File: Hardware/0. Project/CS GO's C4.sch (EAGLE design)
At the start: 47 parts, among them CN1 CELL--PHMC4-02, CN2 ICSP, CN4 TERMINAL-BLOCK-2P-5MM, CN5 TERMINAL-BLOCK-2P-5MM, Q1 NPN-BC817, Q3 N-FET-ENHANCEMENT-SQ2310, SW1 SPST-LATCH-PHMC4-02, U1 1117-3.3V, U4 PCF8574DW, U6 ATMEGA328P-PU, Y1 16 MHz

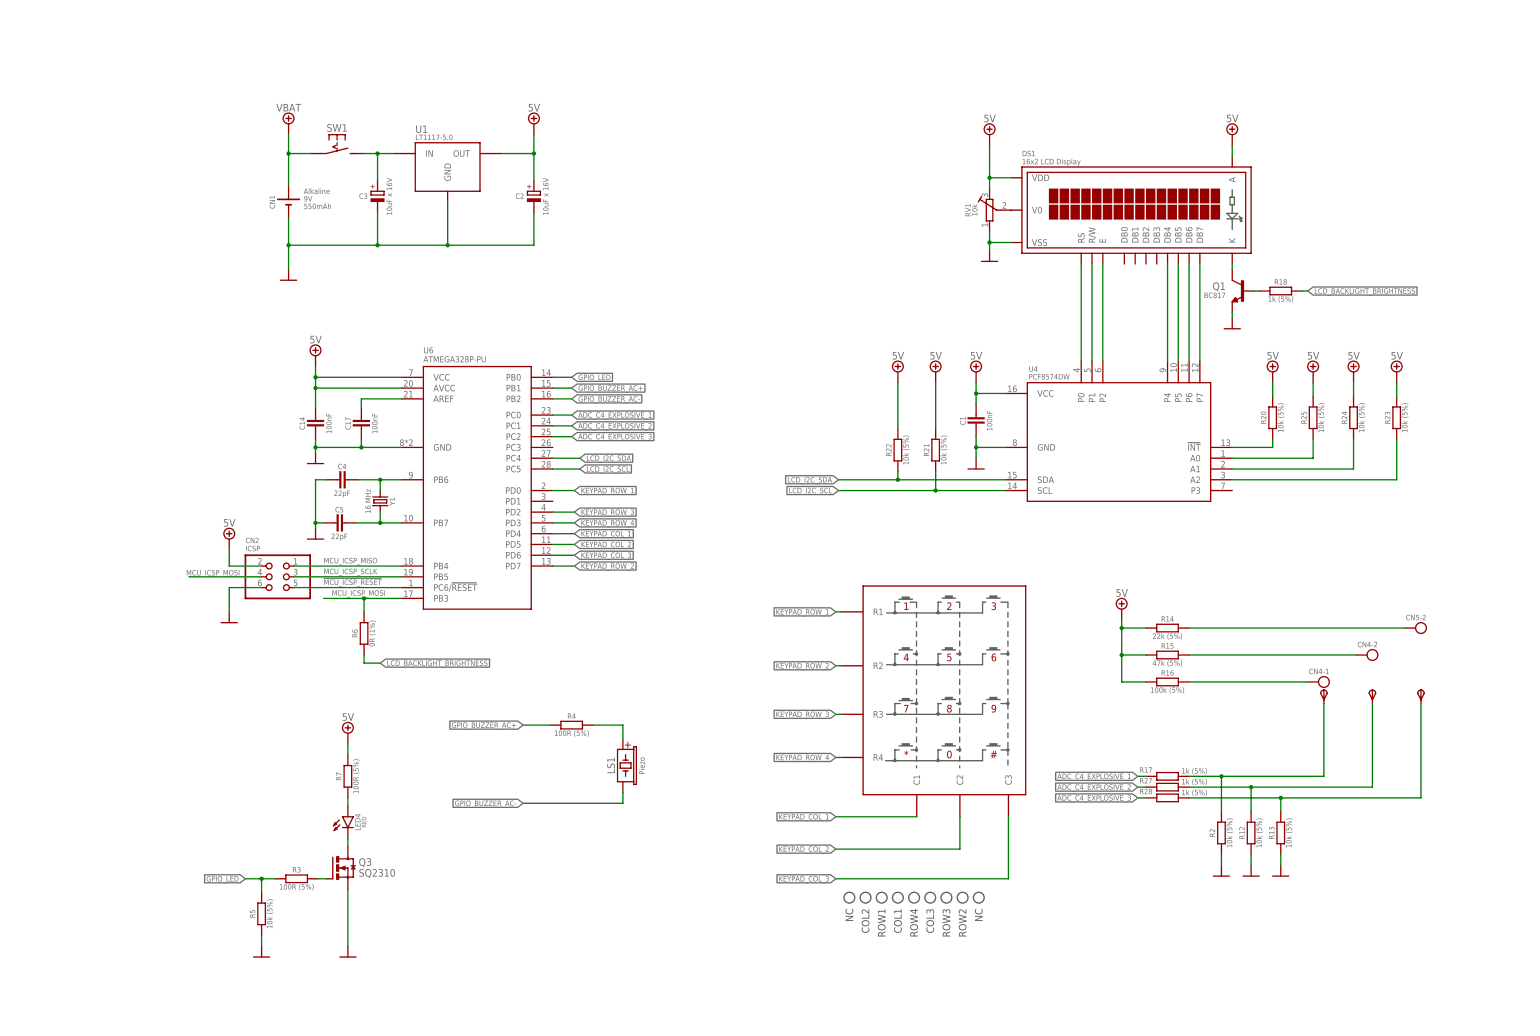
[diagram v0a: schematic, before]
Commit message: PNP BJT added to control LCD backlight brightness
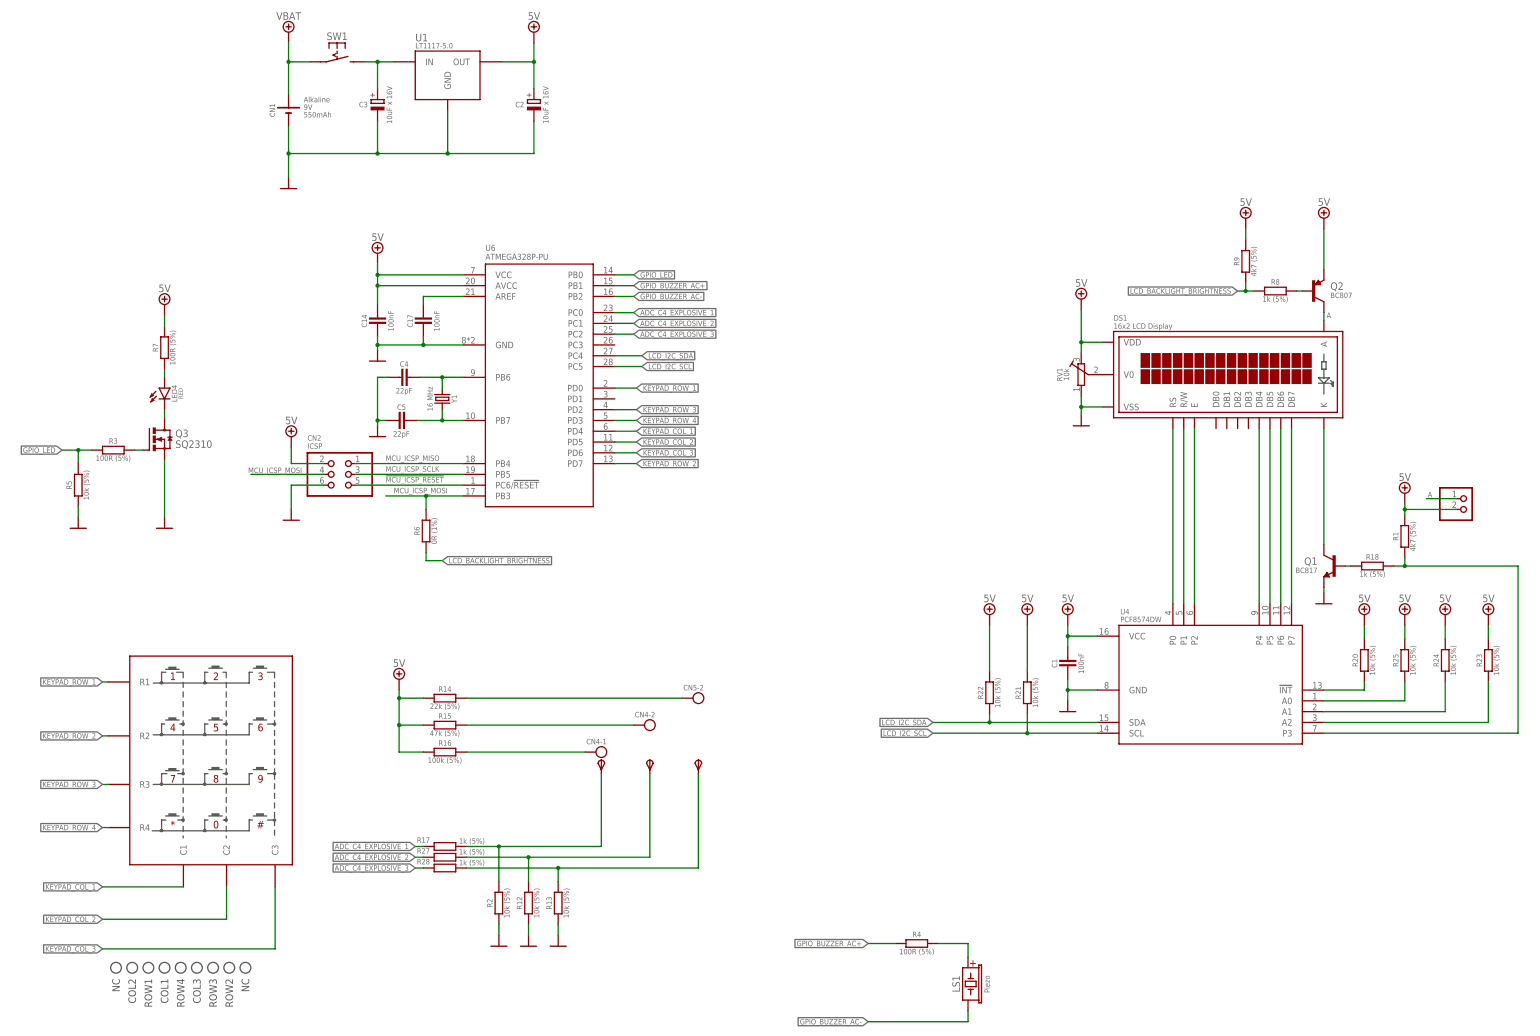
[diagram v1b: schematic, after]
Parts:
- added CN3: (no value), My-PinHeaders:PINHD-1X2
- added Q2: PNP-BC807, My-Transistors:PNP-BC807
- added R1, R9: 4k7 (5%), My-RLC:R_0603
- added R8: 1k (5%), My-RLC:R_0603
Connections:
- new net A: CN3.1, DS1.A, Q2.E
- new net N$15: R1.2, R18.1, U4.P3
- new net N$22: Q2.B, R8.1
- net 5.0V: now also CN3.2, Q2.C, R1.1, R9.1; no longer DS1.A
- net LCD_BACKLIGHT_BRIGHTNESS: now also R8.2, R9.2; no longer R18.1
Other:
- note added: "LCD/I2C PCF8574 BREAKOUT BOARD - EQUIVALENT CIRCUIT"
- note added: "backlight ON/OFF pin header"
- note added: "this pins header must be left open"
- moved on the sheet: C1, C14, C17, C2, C3, C4, C5, CN1, CN2, CN4-1, CN4-2, CN5-2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

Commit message: LED driver removed
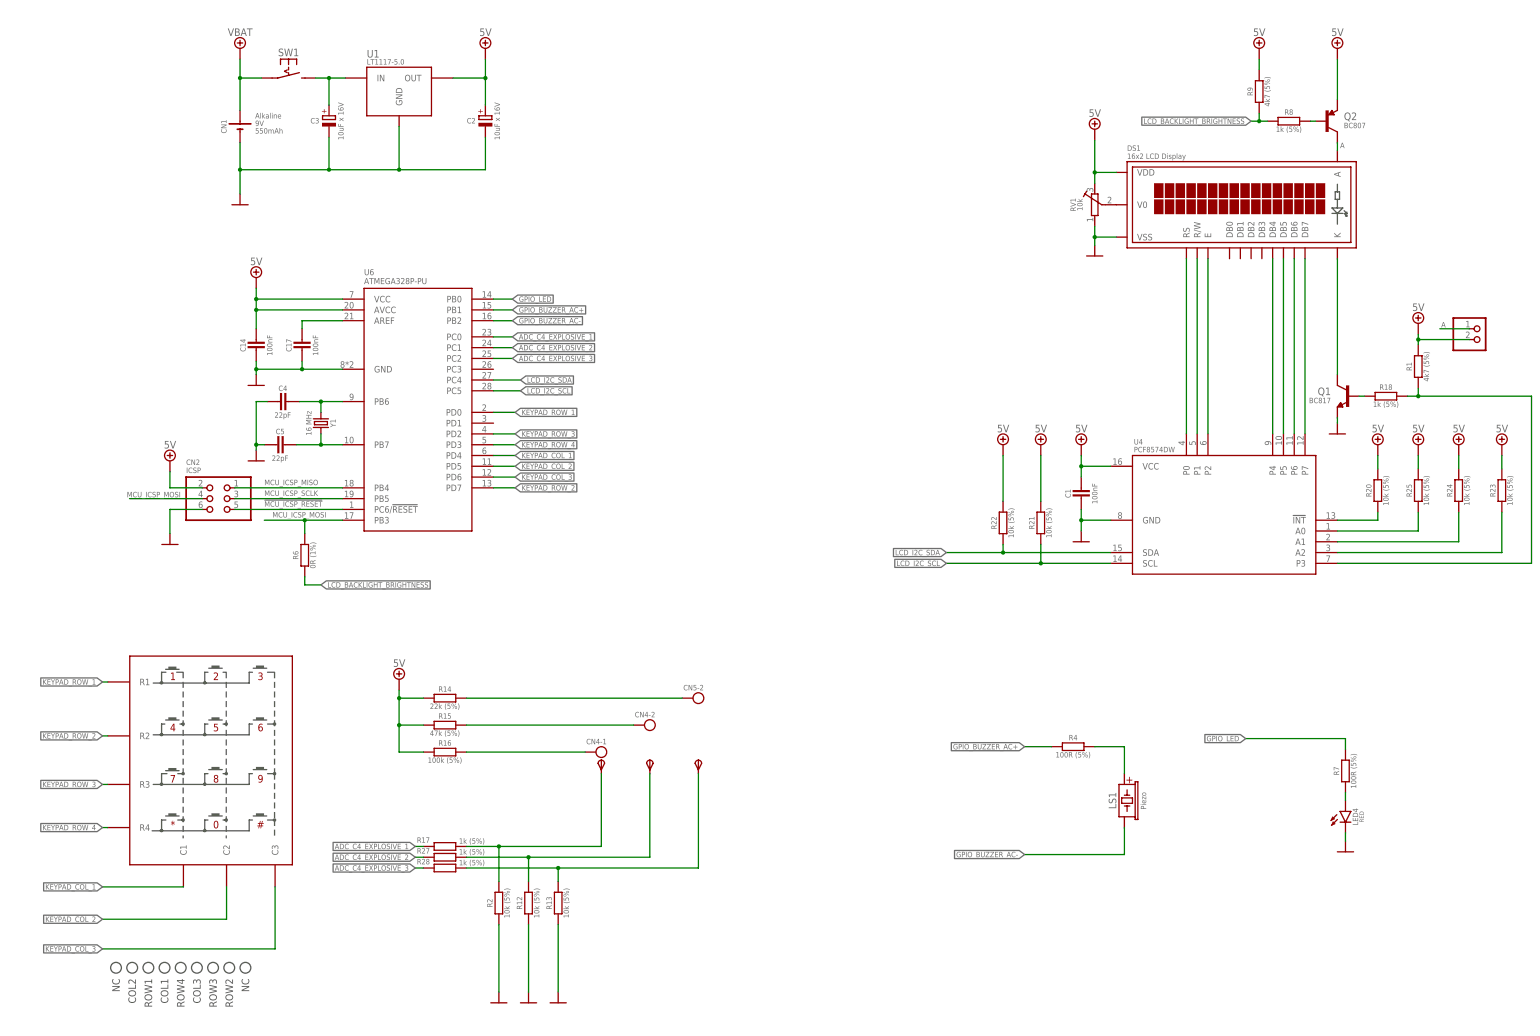
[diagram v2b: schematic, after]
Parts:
- removed Q3: N-FET-ENHANCEMENT-SQ2310, My-Transistors:N-FET-ENHANCEMENT-SQ2310
- removed R3: 100R (5%), My-RLC:R_0603
- removed R5: 10k (5%), My-RLC:R_0603
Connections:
- removed net N$2: LED4.K, Q3.D
- removed net N$3: Q3.G, R3.2
- net 0V: now also LED4.K; no longer Q3.S, R5.1
- net 5.0V: no longer R7.2
- net GPIO_LED: now also R7.2; no longer R3.1, R5.2
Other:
- moved on the sheet: C1, C14, C17, C2, C3, C4, C5, CN1, CN2, DS1, LED4, LS1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
